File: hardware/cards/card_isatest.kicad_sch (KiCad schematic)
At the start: 3 parts, among them M1 Pico (RP2040)

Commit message: card_isatest: add design notes, README entry, and built outputs
Co-Authored-By: Claude Opus 4.8 (1M context) <noreply@anthropic.com>
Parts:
- added C3, C4, C5, C6, C7, C8: 100nF, symbol Device:C
- added D1, D2: D_Schottky, symbol Device:D_Schottky
- added J1: ISA slot (8-bit), symbol Connector:Bus_ISA_8bit
- added J2: ISA SIDECAR, symbol Connector_Generic:Conn_02x30_Odd_Even
- added J3: 5V jack, symbol Connector:Barrel_Jack
- added OSC1: 14.31818MHz, symbol Oscillator:ACO-xxxMHz
- added Q1: Q_PMOS, symbol Device:Q_PMOS
- added R1, R2, R3: 10k, symbol Device:R
- added U1, U2, U3, U4, U5, U6, U7, U8: 74LVC245A, symbol mini-xt:74LVC245A
- added U10, U11, U12, U9: 74HC595, symbol 74xx:74HC595
- added U13, U14: 74HCT165, symbol mini-xt:74HCT165
- added U15: 74HCT74, symbol mini-xt:74HCT74
- added U16: 74HCT163, symbol mini-xt:74HCT163
- added U17, U18: 74HCT157, symbol mini-xt:74HCT157
- added U19: 74HCT04, symbol mini-xt:74HCT04
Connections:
- net +3V3: now also C3.1, C4.1, C5.1, C6.1, R1.2, R3.2, U1.20 (VCC), U10.10 (~{SRCLR}), U10.16 (VCC), U11.10 (~{SRCLR}), U11.16 (VCC), U12.10 (~{SRCLR}), U12.16 (VCC), U13.16 (VCC), U14.16 (VCC), U2.1 (A->B), U2.20 (VCC), U3.1 (A->B), U3.20 (VCC), U4.1 (A->B), U4.20 (VCC), U5.1 (A->B), U5.20 (VCC), U6.1 (A->B), U6.20 (VCC), U7.20 (VCC), U8.20 (VCC), U9.10 (~{SRCLR}), U9.16 (VCC)
- net +5V_USB: now also D2.2 (A)
- net CLK_S: now also U8.6 (A4)
- net DATADIR: now also U1.1 (A->B)
- net GND: now also C3.2, C4.2, C5.2, C6.2, C7.2, C8.2, J1.1 (GND), J1.10 (GND), J1.31 (GND), J2.11 (Pin_11), J2.17 (Pin_17), J2.59 (Pin_59), J3.2, OSC1.7 (GND), U1.10 (GND), U10.13 (~{OE}), U10.8 (GND), U11.13 (~{OE}), U11.8 (GND), U12.13 (~{OE}), U12.8 (GND), U13.15 (~{CE}), U13.8 (GND), U14.10 (DS), U14.14 (D3), U14.15 (~{CE}), U14.3 (D4), U14.4 (D5), U14.5 (D6), U14.6 (D7), U14.8 (GND), U15.7 (GND), U16.4 (D1), U16.8 (GND), U17.15 (E), U17.8 (GND), U18.15 (E), U18.8 (GND), U19.11 (P11), U19.13 (P13), U19.3 (P3), U19.5 (P5), U19.7 (GND), U19.9 (P9), U2.10 (GND), U3.10 (GND), U4.10 (GND), U5.10 (GND), U6.10 (GND), U7.1 (A->B), U7.10 (GND), U8.1 (A->B), U8.10 (GND), U9.13 (~{OE}), U9.8 (GND)
- net IN_PL: now also U13.1 (~{PL}), U14.1 (~{PL})
- net IN_QH: now also U13.9 (Q7)
- net IOCHRDY_S: now also U8.5 (A3)
- net MD0: now also U1.2 (A0)
- net MD1: now also U1.3 (A1)
- net MD2: now also U1.4 (A2)
- net MD3: now also U1.5 (A3)
- net MD4: now also U1.6 (A4)
- net MD5: now also U1.7 (A5)
- net MD6: now also U1.8 (A6)
- net MD7: now also U1.9 (A7)
- net M_IOR: now also U5.4 (A2)
- net M_IOW: now also U5.5 (A3)
- net M_MEMR: now also U5.2 (A0)
- net M_MEMW: now also U5.3 (A1)
- net M_REFRESH: now also U6.5 (A3)
- net PIO_CLK: now also U18.3 (I1a)
- net RCLK_ADDR: now also U10.12 (RCLK), U11.12 (RCLK), U9.12 (RCLK)
- net RCLK_CTRL: now also U12.12 (RCLK)
- net SER: now also U9.14 (SER)
- net SRCLK: now also U10.11 (SRCLK), U11.11 (SRCLK), U12.11 (SRCLK), U13.2 (CP), U14.2 (CP), U9.11 (SRCLK)
- net V5RAW: now also D1.1 (K), D2.1 (K), Q1.S
- net ~{BUF_EN}: now also R1.1, U1.19 (CE), U2.19 (CE), U3.19 (CE), U4.19 (CE), U5.19 (CE), U6.19 (CE), U7.19 (CE), U8.19 (CE)
- new net +5V: C7.1, C8.1, J1.29 (VCC), J1.3 (VCC), J2.3 (Pin_3), J2.55 (Pin_55), OSC1.14 (Vcc), Q1.D, R2.2, U15.1 (~{R}), U15.14 (VCC), U15.4 (~{S}), U16.1 (~{MR}), U16.10 (CET), U16.16 (VCC), U16.3 (D0), U16.5 (D2), U16.6 (D3), U16.7 (CEP), U17.16 (VCC), U18.16 (VCC), U19.14 (VCC)
- new net A0: J1.62 (BA00), J2.60 (Pin_60), U2.18 (B0)
- new net A1: J1.61 (BA01), J2.58 (Pin_58), U2.17 (B1)
- new net A10: J1.52 (BA10), J2.40 (Pin_40), U3.16 (B2)
- new net A11: J1.51 (BA11), J2.38 (Pin_38), U3.15 (B3)
- new net A12: J1.50 (BA12), J2.36 (Pin_36), U3.14 (B4)
- new net A13: J1.49 (BA13), J2.34 (Pin_34), U3.13 (B5)
- new net A14: J1.48 (BA14), J2.32 (Pin_32), U3.12 (B6)
- new net A15: J1.47 (BA15), J2.30 (Pin_30), U3.11 (B7)
- new net A16: J1.46 (BA16), J2.28 (Pin_28), U4.18 (B0)
- new net A17: J1.45 (BA17), J2.26 (Pin_26), U4.17 (B1)
- new net A18: J1.44 (BA18), J2.24 (Pin_24), U4.16 (B2)
- new net A19: J1.43 (BA19), J2.22 (Pin_22), U4.15 (B3)
- new net A2: J1.60 (BA02), J2.56 (Pin_56), U2.16 (B2)
- new net A3: J1.59 (BA03), J2.54 (Pin_54), U2.15 (B3)
- new net A4: J1.58 (BA04), J2.52 (Pin_52), U2.14 (B4)
- new net A5: J1.57 (BA05), J2.50 (Pin_50), U2.13 (B5)
- new net A6: J1.56 (BA06), J2.48 (Pin_48), U2.12 (B6)
- new net A7: J1.55 (BA07), J2.46 (Pin_46), U2.11 (B7)
- new net A8: J1.54 (BA08), J2.44 (Pin_44), U3.18 (B0)
- new net A9: J1.53 (BA09), J2.42 (Pin_42), U3.17 (B1)
- new net AEN: J1.42 (AEN), J2.20 (Pin_20), U5.14 (B4)
- new net BALE: J1.28 (ALE), J2.53 (Pin_53), U5.11 (B7)
- new net CLK: J1.20 (CLK), J2.37 (Pin_37), U19.2 (P2), U8.14 (B4)
- new net CLK4: U16.14 (Q0), U17.3 (I1a)
- new net CLK7: U15.5 (Q), U17.2 (I0a)
- new net CLK_HW: U17.4 (Za), U18.2 (I0a)
- new net CLK_PRE: U18.4 (Za), U19.1 (P1)
- new net CLK_QN: U15.2 (D), U15.6 (~{Q})
- new net CLK_SRC: U11.5 (QF), U18.1 (S)
- new net D0: J1.40 (DB0), J2.16 (Pin_16), U1.18 (B0)
- new net D1: J1.39 (DB1), J2.14 (Pin_14), U1.17 (B1)
- new net D2: J1.38 (DB2), J2.12 (Pin_12), U1.16 (B2)
- new net D3: J1.37 (DB3), J2.10 (Pin_10), U1.15 (B3)
- new net D4: J1.36 (DB4), J2.8 (Pin_8), U1.14 (B4)
- new net D5: J1.35 (DB5), J2.6 (Pin_6), U1.13 (B5)
- new net D6: J1.34 (DB6), J2.4 (Pin_4), U1.12 (B6)
- new net D7: J1.33 (DB7), J2.2 (Pin_2), U1.11 (B7)
- new net DIV3_LD: U16.9 (~{PE})
- new net DIV3_TC: U16.15 (TC)
- new net DRQ1: J1.18 (DRQ1), J2.33 (Pin_33), U7.11 (B7)
- new net DRQ1_S: U13.6 (D7), U7.9 (A7)
- new net DRQ2: J1.6 (DRQ2), J2.9 (Pin_9), U8.18 (B0)
- new net DRQ2_S: U14.11 (D0), U8.2 (A0)
- new net DRQ3: J1.16 (DRQ3), J2.29 (Pin_29), U8.17 (B1)
- new net DRQ3_S: U14.12 (D1), U8.3 (A1)
- new net DUT_PWR_EN: Q1.G, R3.1, U11.6 (QG)
- new net IN_CASCADE: U13.10 (DS), U14.9 (Q7)
- new net IOCHCK_S: U14.13 (D2), U8.4 (A2)
- new net IOCHRDY: J1.41 (IO_READY), J2.18 (Pin_18), R2.1, U8.15 (B3)
- new net IRQ2: J1.4 (IRQ2), J2.5 (Pin_5), U7.18 (B0)
- new net IRQ2_S: U13.11 (D0), U7.2 (A0)
- new net IRQ3: J1.25 (IRQ3), J2.47 (Pin_47), U7.17 (B1)
- new net IRQ3_S: U13.12 (D1), U7.3 (A1)
- new net IRQ4: J1.24 (IRQ4), J2.45 (Pin_45), U7.16 (B2)
- new net IRQ4_S: U13.13 (D2), U7.4 (A2)
- new net IRQ5: J1.23 (IRQ5), J2.43 (Pin_43), U7.15 (B3)
- new net IRQ5_S: U13.14 (D3), U7.5 (A3)
- new net IRQ6: J1.22 (IRQ6), J2.41 (Pin_41), U7.14 (B4)
- new net IRQ6_S: U13.3 (D4), U7.6 (A4)
- new net IRQ7: J1.21 (IRQ7), J2.39 (Pin_39), U7.13 (B5)
- new net IRQ7_S: U13.4 (D5), U7.7 (A5)
- new net IRQ8: J2.15 (Pin_15), U7.12 (B6)
- new net IRQ8_S: U13.5 (D6), U7.8 (A6)
- new net MA0: U2.2 (A0), U9.15 (QA)
- new net MA1: U2.3 (A1), U9.1 (QB)
- new net MA10: U10.2 (QC), U3.4 (A2)
- new net MA11: U10.3 (QD), U3.5 (A3)
- new net MA12: U10.4 (QE), U3.6 (A4)
- new net MA13: U10.5 (QF), U3.7 (A5)
- new net MA14: U10.6 (QG), U3.8 (A6)
- new net MA15: U10.7 (QH), U3.9 (A7)
- new net MA16: U11.15 (QA), U4.2 (A0)
- new net MA17: U11.1 (QB), U4.3 (A1)
- new net MA18: U11.2 (QC), U4.4 (A2)
- new net MA19: U11.3 (QD), U4.5 (A3)
- new net MA2: U2.4 (A2), U9.2 (QC)
- new net MA3: U2.5 (A3), U9.3 (QD)
- new net MA4: U2.6 (A4), U9.4 (QE)
- new net MA5: U2.7 (A5), U9.5 (QF)
- new net MA6: U2.8 (A6), U9.6 (QG)
- new net MA7: U2.9 (A7), U9.7 (QH)
- new net MA8: U10.15 (QA), U3.2 (A0)
- new net MA9: U10.1 (QB), U3.3 (A1)
- new net M_AEN: U12.15 (QA), U5.6 (A4)
- new net M_BALE: U12.6 (QG), U5.9 (A7)
- new net M_DACK1: U12.3 (QD), U6.2 (A0)
- new net M_DACK2: U12.4 (QE), U6.3 (A1)
- new net M_DACK3: U12.5 (QF), U6.4 (A2)
- new net M_RESETDRV: U12.1 (QB), U5.7 (A5)
- new net M_TC: U12.2 (QC), U5.8 (A6)
- new net OSC: J1.30 (OSC), J2.57 (Pin_57), OSC1.8 (OUT), U15.3 (C), U16.2 (CP)
- new net RESET_DRV: J1.2 (RESET), J2.1 (Pin_1), U5.13 (B5)
- new net SER_A01: U10.14 (SER), U9.9 (QH')
- new net SER_A12: U10.9 (QH'), U11.14 (SER)
- new net SER_A2C: U11.9 (QH'), U12.14 (SER)
- new net SPEED_SEL: U11.4 (QE), U17.1 (S)
- new net TC: J1.27 (TC), J2.51 (Pin_51), U5.12 (B6)
- new net VEXT: D1.2 (A), J3.1
- new net ~{DACK1}: J1.17 (~{DACK1}), J2.31 (Pin_31), U6.18 (B0)
- new net ~{DACK2}: J1.26 (~{DACK2}), J2.49 (Pin_49), U6.17 (B1)
- new net ~{DACK3}: J1.15 (~{DACK3}), J2.27 (Pin_27), U6.16 (B2)
- new net ~{IOCHCK}: J1.32 (IO), J2.7 (Pin_7), U8.16 (B2)
- new net ~{IOR}: J1.14 (~{IOR}), J2.25 (Pin_25), U5.16 (B2)
- new net ~{IOW}: J1.13 (~{IOW}), J2.23 (Pin_23), U5.15 (B3)
- new net ~{MEMR}: J1.12 (~{SMEMR}), J2.21 (Pin_21), U5.18 (B0)
- new net ~{MEMW}: J1.11 (~{SMEMW}), J2.19 (Pin_19), U5.17 (B1)
- new net ~{REFRESH}: J1.19 (~{DACK0}), J2.35 (Pin_35), U6.15 (B3)
- no-connect marks 5 -> 42
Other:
- note added: "Clock: 14.318 OSC -> /2 (U15) & /3 (U16) -> SPEED_SEL mux (U17) -> CLK_SRC mux (U18, PIO override) -> buffer (U19) -> bus CLK. CLK sensed back to Pico via U8 (CLK_S). /3 preset per cpu_core."
- note added: "IN chain: IRQ2-8 / DRQ1-3 / IOCHCK# -> IN_QH (U14 cascades into U13). Sampled occasionally; off the hot path."
- note added: "OUT chain: address (U9-U11, RCLK_ADDR) + control byte (U12, RCLK_CTRL). Address-only updates shift 24b; controls stay latched."
- note added: "Power: USB 5V (logic) + external jack (bus/DUT) OR-ed via D1/D2 to V5RAW; Q1 P-FET (DUT_PWR_EN) switches bus +5V. See questions doc for gate-drive/level detail."

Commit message: Fix all critical+high design-review findings (C1-C5, H1-H8)
Full review in hardware/notes/design-review-2026-07-03.md (with per-item
fix logs). Highlights:
- SRAM strobed by gated MEMR/MEMW (was raw ~RD/~WR: I/O cycles corrupted
  SRAM and the boot shadow-load could never write it)
- Reset chain implemented: NAND combine of ~PWRGOOD + ~CPURESET drives
  V20 RESET and an always-driven RESET_DRV (dropped from the Bus MCU)
- Contention-free bus handoff: '573 OE=HLDA vs counter '244 stage
  ~OE=~HLDA; strobe gates wired + tri-stated ('125, ~OE=HLDA); Bus MCU
  address group fixed to sense; AEN/TC fixed drive; BALE input-only
- '573 LE driven by BALE (was a dangling BALE_L label)
- Data '245 DIR=DT/~R, ~OE=DEN so INTA vectors reach the CPU
- Idle pulls: strobes/DEN high, AEN/IRQ2-9/DRQ low, IOCHRDY/IOCHCK/
  DACK2-3 high
- CH224K CFG1 left open (grounding it selects 9-20V, not 5V)
- XT-IDE INTRQ pull-down (pull-up parked IRQ5 asserted)
- LPT status bit7 = ~Busy via spare inverter (SPP semantics)
- Audio summer TL072 -> MCP6002 (RRIO; TL072 out of spec at +5V single
  supply)
- card_isatest: DUT P-FET gate to V5RAW + NPN driver (default off, can
  fully turn off); /3 divider TC->~PE reload actually wired

Overturned picks corrected in notes/questions-*.md. All sheets + cards
rebuilt; structural ERC = 0; fixes netlist-verified.

Co-Authored-By: Claude Fable 5 <noreply@anthropic.com>
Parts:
- added Q2: 2N3904, symbol Transistor_BJT:2N3904
- added R4: 4.7k, symbol Device:R
- added R5: 10k, symbol Device:R
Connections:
- net +3V3: no longer R3.2
- net DIV3_LD: now also U19.4 (P4)
- net DIV3_TC: now also U19.3 (P3)
- net DUT_PWR_EN: now also R4.1; no longer Q1.G
- net GND: now also R3.2, Q2.1 (E); no longer U19.3 (P3)
- net V5RAW: now also R5.2
- new net PFET_B: Q2.2 (B), R4.2
- new net PFET_G: Q1.G, Q2.3 (C), R5.1
- no-connect marks 42 -> 41
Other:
- note added: "Power: USB 5V (logic) + external jack (bus/DUT) OR-ed via D1/D2 to V5RAW; Q1 P-FET switches bus +5V. Gate pulled to V5RAW (off), pulled low by Q2 NPN when DUT_PWR_EN=1."
- note removed: "Power: USB 5V (logic) + external jack (bus/DUT) OR-ed via D1/D2 to V5RAW; Q1 P-FET (DUT_PWR_EN) switches bus +5V. See questions doc for gate-drive/level detail."

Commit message: Fix all medium design-review findings (M1-M8)
- M1: Supervisor link moved to GPIO4/5 (real UART1 pair); POST -> GPIO6-15
- M2: CNT_RUN = LD0.LD1.LD2 gates every '163 CEP (load-cascade hazard)
- M3: ~WR / IO-M pruned to cpu_core-internal; DRQ2/3 pulled + noted;
  doc S5.2 "as built: 48/48" + S16 updated
- M4: true XT-IDE rev-2 map (A0<->A3 swap): data 0x300, latch 0x301,
  CS1 0x307/0x30F, drive DA0 = bus A3 - matches XTIDE UB "rev 2" type
- M5: COM4 -> bus IRQ2 line (IRQ9 via AT redirect); IRQ10/11/14/15 marked
  off-header; ~REFRESH added to mxbus ISA_CTRL; questions-sidecar superseded
- M6: card_isatest clock tree on unswitched V5RAW (spec S8)
- M7: card_isatest IRQ2-8/DRQ1-3 idle pull-downs (spec S4/S9)
- M8: com_port JP1 selects 16550 RX source (DB9 vs TTL console); 5V note

Rebuilt motherboard + cards; structural ERC = 0; netlist-verified.
Fix log in hardware/notes/design-review-2026-07-03.md (batch 3).

Co-Authored-By: Claude Fable 5 <noreply@anthropic.com>
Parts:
- added R10, R11, R12, R13, R14, R15, R6, R7, R8, R9: 10k, symbol Device:R
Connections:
- net DRQ2 is gone; now on net GND: J1.6 (DRQ2), J2.9 (Pin_9), U8.18 (B0)
- net RESET_DRV is gone; now on net DRQ3: J1.2 (RESET), J2.1 (Pin_1), U5.13 (B5)
- net +5V: no longer C7.1, OSC1.14 (Vcc), U15.1 (~{R}), U15.14 (VCC), U15.4 (~{S}), U16.1 (~{MR}), U16.10 (CET), U16.16 (VCC), U16.3 (D0), U16.5 (D2), U16.6 (D3), U16.7 (CEP), U17.16 (VCC), U18.16 (VCC), U19.14 (VCC)
- net DRQ1: now also R13.1
- net DRQ3: now also R15.1
- net GND: now also R10.2, R11.2, R12.2, R13.2, R14.1, R14.2, R15.2, R6.2, R7.2, R8.2, R9.2
- net IRQ2: now also R6.1
- net IRQ3: now also R7.1
- net IRQ4: now also R8.1
- net IRQ5: now also R9.1
- net IRQ6: now also R10.1
- net IRQ7: now also R11.1
- net IRQ8: now also R12.1
- net V5RAW: now also C7.1, OSC1.14 (Vcc), U15.1 (~{R}), U15.14 (VCC), U15.4 (~{S}), U16.1 (~{MR}), U16.10 (CET), U16.16 (VCC), U16.3 (D0), U16.5 (D2), U16.6 (D3), U16.7 (CEP), U17.16 (VCC), U18.16 (VCC), U19.14 (VCC)

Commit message: Fix all low-severity + toolchain design-review findings
Low:
- LPT IRQ7 via tri-state '125 (NAND-enabled ack pulse) - shareable line
- card_com JP2 IRQ strap follows the base-address strap (was IRQ4-only)
- Supervisor USB-A VBUS fused (500mA polyfuse)
- card_isatest: DUT_PWR_EN moved to the control '595 (addr shifts can't
  glitch DUT power); '165s -> 74HC grade (HCT needs VCC 4.5-5.5V)
- /3 duty comments corrected; U13 marked load-bearing inverting buffer
- RTC AS hold-path bench note; duplicate ~RD stub removed
- mxbus PRIV_DECODE emptied (Y5 never leaves cpu_core)

Toolchain:
- build.py/build_cards return real exit codes, failing on structural ERC
  (endpoint_off_grid/unconnected_wire_endpoint/multiple_net_names) or a
  failed netlist export
- KiCad paths resolved via mxsch.kicad_cli()/kicad_symdir() (env, PATH,
  snap `current`) - no pinned snap revision anywhere
- Deterministic UUIDs (uuid5 title-seed + counter): rebuilds are
  byte-identical (verified); this rewrites every UUID once
- S-expression string escapes now round-trip (parse decodes, dump encodes)
- CLAUDE.md updated to match

The new structural gate immediately caught its own batch's bug (pull row
placed inside card_isatest's J2 pin field) - moved and re-verified.

Co-Authored-By: Claude Fable 5 <noreply@anthropic.com>
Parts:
- U13, U14: value 74HCT165 -> 74HC165
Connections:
- net DRQ3: no longer J1.2 (RESET), J2.1 (Pin_1), U5.13 (B5)
- net DUT_PWR_EN: now also U12.7 (QH); no longer U11.6 (QG)
- net GND: no longer J1.6 (DRQ2), J2.9 (Pin_9), R14.1, U8.18 (B0)
- new net DRQ2: J1.6 (DRQ2), J2.9 (Pin_9), R14.1, U8.18 (B0)
- new net RESET_DRV: J1.2 (RESET), J2.1 (Pin_1), U5.13 (B5)

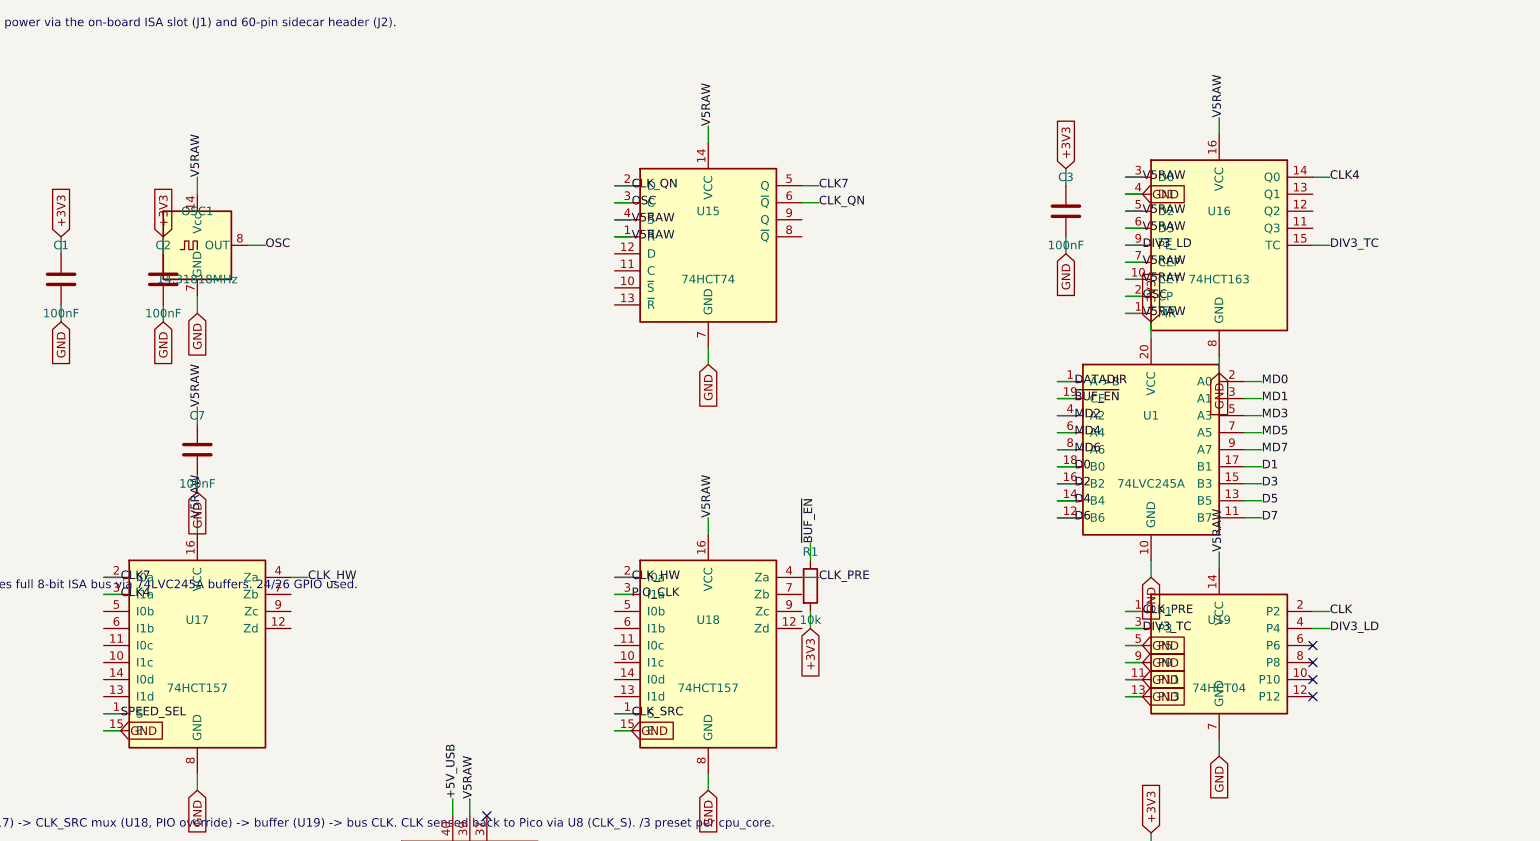
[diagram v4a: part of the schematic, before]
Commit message: JLCPCB sourcing pass: verify pinouts, LCSC part numbers, SMD build
Custom-symbol verification (open-questions Q5 resolved):
- MAX3241 symbol was wrong on nearly every pin and used MAX3243-style
  control names; regenerated to the real SSOP-28 pinout (SHDN#/EN#/
  R1OUTB/R2OUTB) and com_port rewired -- EN# must be GROUNDED (the old
  ~FORCEON-high would have disabled the receivers on real silicon)
- DS12C887 symbol wrong on 4 pins (DS=17, RESET#=18, IRQ#=19, SQW=23)

Sourcing (every part checked against the JLC DB; ~45 line items):
- New tools/parts.py maps (lib_id, value) -> LCSC; build.py applies it as
  an 'LCSC Part Num' property on every component (384 across the project)
- Sheets stay generic; stock-forced substitutions bound in the map:
  '374->'574 (parallel rewired), '163->'161, '157->HC157 (+HCT-buffered
  3.3V selects, I0/I1 swapped), '02->HC02, TCM809->MCP809, 2N3904->MMBT3904
- bus_mcu address counters moved to the 3.3V domain (HC161 on 3V3_BUS,
  loaded from MCU-side MD0-7; HCT244s read the 3.3V outputs at TTL Vih)
- 14.318 XOs are 3.3V-only parts: powered from 3V3, squared up via spare
  HCT gates (cpu_core U13, card_isatest U19)
- COM baud reference is now a 1.8432MHz crystal on the 16C550's XIN/XOUT
  (3.3V-only oscillators vs a 5V-only soft card)
- Supervisor QSPI header replaced with a real W25Q128JVSIQ
- Socket policy (fab installs sockets): V20 DIP-40, SRAM DIP-32 (no 5V
  512Kx8 SRAM at JLC at all), DS12C887 DIP-24, female headers for modules

Docs: CLAUDE.md fabrication-constraints section (SMD, 100x100mm, generic-
symbols rule, voltage-domain rule); README + hardware/README fab notes;
notes/jlcpcb-sourcing.md (decisions, thin-stock flags, not-at-JLC list);
stale questions-sidecar.md collapsed to its supersession record.

Rebuilt motherboard + cards: structural ERC 0, byte-identical rebuilds.

Co-Authored-By: Claude Fable 5 <noreply@anthropic.com>
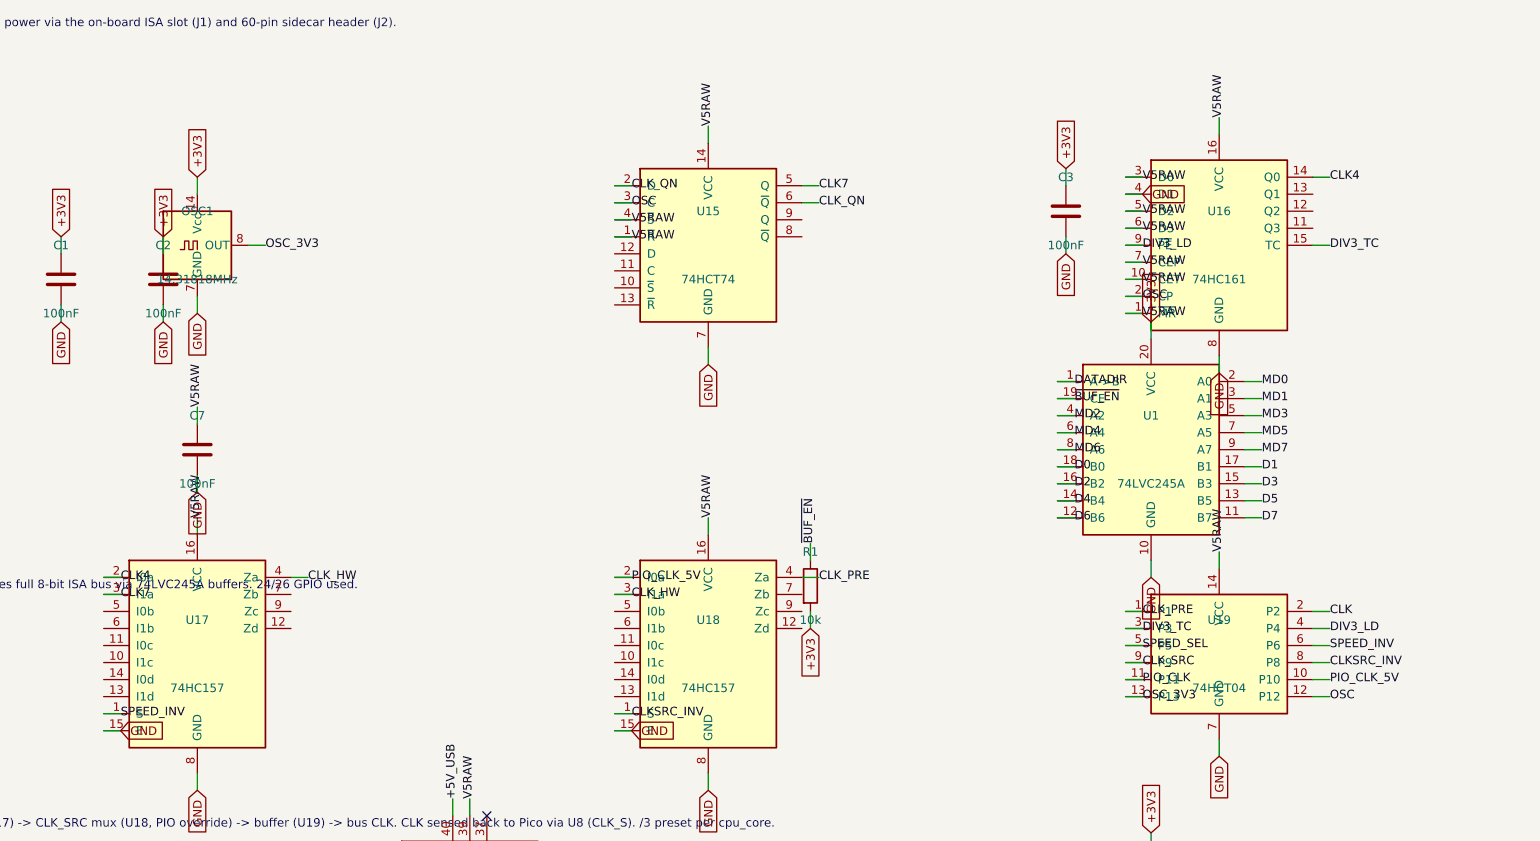
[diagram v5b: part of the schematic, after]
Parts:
- C1, C2, C3, C4, C5, C6, C7, C8: LCSC Part Num (none) -> C14663
- D1, D2: LCSC Part Num (none) -> C8678
- J2: LCSC Part Num (none) -> C2333
- J3: LCSC Part Num (none) -> C2880552
- M1: LCSC Part Num (none) -> C2897411
- OSC1: LCSC Part Num (none) -> C49330311
- Q1: LCSC Part Num (none) -> C15127
- Q2: LCSC Part Num (none) -> C20526
- R1, R10, R11, R12, R13, R14, R15, R2, R3, R5, R6, R7, R8, R9: LCSC Part Num (none) -> C25804
- R4: LCSC Part Num (none) -> C23162
- U1, U2, U3, U4, U5, U6, U7, U8: LCSC Part Num (none) -> C6082
- U10, U11, U12, U9: LCSC Part Num (none) -> C5947
- U13, U14: LCSC Part Num (none) -> C5613
- U15: LCSC Part Num (none) -> C686657
- U16: value 74HCT163 -> 74HC161; LCSC Part Num (none) -> C5610
- U17, U18: value 74HCT157 -> 74HC157; LCSC Part Num (none) -> C5609
- U19: LCSC Part Num (none) -> C672096
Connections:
- net +3V3: now also OSC1.14 (Vcc)
- net CLK4: now also U17.2 (I0a); no longer U17.3 (I1a)
- net CLK7: now also U17.3 (I1a); no longer U17.2 (I0a)
- net CLK_HW: now also U18.3 (I1a); no longer U18.2 (I0a)
- net CLK_SRC: now also U19.9 (P9); no longer U18.1 (S)
- net GND: no longer U19.11 (P11), U19.13 (P13), U19.5 (P5), U19.9 (P9)
- net OSC: now also U19.12 (P12); no longer OSC1.8 (OUT)
- net PIO_CLK: now also U19.11 (P11); no longer U18.3 (I1a)
- net SPEED_SEL: now also U19.5 (P5); no longer U17.1 (S)
- net V5RAW: no longer OSC1.14 (Vcc)
- net PIO_CLK_5V: now reaches U19.10 (P10)
- net PIO_CLK_5V: now also U18.2 (I0a)
- net SPEED_INV: now reaches U19.6 (P6)
- net SPEED_INV: now also U17.1 (S)
- net CLKSRC_INV: now reaches U19.8 (P8)
- net CLKSRC_INV: now also U18.1 (S)
- new net OSC_3V3: OSC1.8 (OUT), U19.13 (P13)
- no-connect marks 41 -> 37
